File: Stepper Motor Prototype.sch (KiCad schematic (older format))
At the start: 64 parts, among them J1 USB_B_Micro, J2 Screw_Terminal_01x02, J3 Screw_Terminal_01x04, Q1 STD20NF06L, Q2 STD20NF06L, Q3 STD20NF06L, Q4 STD20NF06L, Q5 STD20NF06L, Q6 STD20NF06L, Q7 STD20NF06L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

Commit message: added logic level shifters
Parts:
- removed C16: C, Capacitors_SMD:C_0603_HandSoldering, symbol Device:C
- removed C17, C18, C19, C20, C21, C22, C23, C24: 0.1uF, Capacitors_SMD:C_0603_HandSoldering, symbol Device:C
- removed D1: SP0502BAHT, TO_SOT_Packages_SMD:SOT-23, symbol Power_Protection:SP0502BAHT
- removed D2: TX_LED, LEDs:LED_1206_HandSoldering, symbol Device:LED
- removed D3: RX_LED, LEDs:LED_1206_HandSoldering, symbol Device:LED
- removed D4: D_Schottky, digikey-footprints:DO-214AB, symbol Device:D_Schottky
- removed D5: LED, LEDs:LED_1206_HandSoldering, symbol Device:LED
- removed J1: USB_B_Micro, Connectors:USB_Mini-B, symbol Connector:USB_B_Micro
- removed L1: 100uH, my_inductors:Wurth_SMD_Inductor_7447709101, symbol Device:L
- removed U1: FT232RL, Housings_SSOP:TSSOP-28_4.4x9.7mm_Pitch0.65mm, symbol Interface_USB:FT232RL
- removed U2: ESP8266EX, Housings_DFN_QFN:QFN-32-1EP_5x5mm_Pitch0.5mm, symbol MCU_Espressif:ESP8266EX
- removed U3: LM2595SX-3.3_NOPB, TO_SOT_Packages_SMD:TO-263-5_TabPin3, symbol Voltage~Regulators:LM2595SX-3.3_NOPB
- removed U5: LM2595SX-5.0_NOPB, TO_SOT_Packages_SMD:TO-263-5_TabPin3, symbol Voltage~Regulators:LM2595SX-5.0_NOPB
- removed U6: S25FL512SAGMFIG11, Housings_SOIC:SOIC-16_3.9x9.9mm_Pitch1.27mm, symbol Memory_Flash_3DP:S25FL512SAGMFIG11
- removed U8: STM32F407VGTx, Housings_QFP:LQFP-100_14x14mm_Pitch0.5mm, symbol MCU_ST_STM32F4:STM32F407VGTx
- removed Y1: Crystal_GND24, Crystals:Crystal_SMD_SeikoEpson_TSX3225-4pin_3.2x2.5mm, symbol Device:Crystal_GND24
- added J1: Conn_01x15, Pin_Headers:Pin_Header_Straight_1x15_Pitch1.27mm, symbol Connector_Generic:Conn_01x15
- added R9: 10k, Resistors_SMD:R_0603_HandSoldering, symbol Device:R
- added U1: LM2595SX-5.0_NOPB, TO_SOT_Packages_SMD:TO-263-5_TabPin3, symbol VoltageRegulators:LM2595SX-5.0_NOPB
- added U2, U3: SN74AXC8T245, Housings_SSOP:TSSOP-24_4.4x7.8mm_Pitch0.65mm, symbol logic_level_shifter_mdg:SN74AXC8T245
- C10: value 4.7uF -> 0.1uF
- C11: value 120uF -> 0.1uF; footprint Capacitors_THT:CP_Radial_D8.0mm_P3.50mm -> Capacitors_SMD:C_0603_HandSoldering
- C12: value 150uF -> 100uF
- C15: value C -> 1uF
- C9: value 0.1uF -> 100uF; footprint Capacitors_SMD:C_0603_HandSoldering -> Capacitors_THT:CP_Radial_D8.0mm_P3.50mm
- R1, R5, R6: value 330R -> 10k
- R3: value 4k7 -> 10k
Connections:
- net labels added: +1V8
- net labels removed: FTDI_BYPASS, ST_P100, ST_P11, ST_P19, ST_P22, ST_P28, ST_P50, ST_P6, ST_P75
- wire segments 208 -> 215
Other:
- moved on the sheet: C1, C2, C4, C5, J2

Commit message: removed power supply, basic layout of 1 motor winding complete
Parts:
- removed C13: 120uF, Capacitors_THT:CP_Radial_D8.0mm_P3.50mm, symbol Device:C
- removed C14: 150uF, Capacitors_THT:CP_Radial_D8.0mm_P3.50mm, symbol Device:C
- removed D6: D_Schottky, digikey-footprints:DO-214AB, symbol Device:D_Schottky
- removed D7: LED, LEDs:LED_1206_HandSoldering, symbol Device:LED
- removed J1: Conn_01x15, Pin_Headers:Pin_Header_Straight_1x15_Pitch1.27mm, symbol Connector_Generic:Conn_01x15
- removed L2: L, my_inductors:Wurth_SMD_Inductor_7447709101, symbol Device:L
- removed R2: 330R, Resistors_SMD:R_0603_HandSoldering, symbol Device:R
- removed U1: LM2595SX-5.0_NOPB, TO_SOT_Packages_SMD:TO-263-5_TabPin3, symbol VoltageRegulators:LM2595SX-5.0_NOPB
- added J1: Conn_01x16, symbol Connector_Generic:Conn_01x16
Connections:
- net +1V8: now also J1.2 (Pin_2)
- net +3V3: now also J1.3 (Pin_3)
- net GND: now also J1.1 (Pin_1)
- net AOUT2: now reaches J3.2 (Pin_2), Q3.2 (D), Q4.3 (S), U7.30 (AOUT2)
- net A2HS: now reaches Q4.1 (G), U7.31 (A2HS)
- net A2LS: now reaches Q3.1 (G), U7.32 (A2LS)
- net A1SENP: now reaches Q2.3 (S), Q3.3 (S), R7.1, U7.34 (AISENP)
- net A1LS: now reaches Q2.1 (G), U7.35 (A1LS)
- net A1HS: now reaches Q1.1 (G), U7.36 (A1HS)
- net AOUT1: now reaches J3.1 (Pin_1), Q1.3 (S), Q2.2 (D), U7.37 (AOUT1)
- net at U2.8 (A6): now also J1.11 (Pin_11)
- net at U2.7 (A5): now also J1.12 (Pin_12)
- net at U2.6 (A4): now also J1.13 (Pin_13)
- net at U2.5 (A3): now also J1.14 (Pin_14)
- net at U2.4 (A2): now also J1.15 (Pin_15)
- net at U2.3 (A1): now also J1.16 (Pin_16)
- net at U3.9 (A7): now also J1.4 (Pin_4)
- net at U3.8 (A6): now also J1.5 (Pin_5)
- net at U3.7 (A5): now also J1.6 (Pin_6)
- net at U3.6 (A4): now also J1.7 (Pin_7)
- net at U3.5 (A3): now also J1.8 (Pin_8)
- net at U3.4 (A2): now also J1.9 (Pin_9)
- net at U3.3 (A1): now also J1.10 (Pin_10)
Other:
- moved on the sheet: J2

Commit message: continued working on motor power section.  Still need to layout mirrored side.
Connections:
- net at Q6.3 (S), Q7.3 (S), R8.1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: no longer J3.4 (Pin_4), U7.21 (BOUT2)
- net at Q7.2 (D), Q8.3 (S): now also J3.4 (Pin_4), U7.21 (BOUT2)
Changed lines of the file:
@@
 	24350 8900 24350 8950
 Wire Wire Line
-	25650 9650 25650 7300
-Wire Wire Line
 	25650 7300 25950 7300
 Wire Wire Line
@@
 	21800 7700 22250 7700
 Wire Wire Line
-	22250 7700 22250 9400
-Wire Wire Line
-	22250 9400 24350 9400
-Connection ~ 24350 9400
-Wire Wire Line
-	24350 9400 24350 9350
-Wire Wire Line
-	24350 10200 24350 10350
-Wire Wire Line
-	25650 9650 24350 9650
-Connection ~ 24350 9650
-Wire Wire Line
-	24350 9650 24350 9500
+	24350 10200 24350 10250
 Connection ~ 24350 9750
-Wire Wire Line
-	24350 9750 24350 9650
 $Comp
 L power:GND #PWR0133
@@
 	22800 9500 24350 9500
 Connection ~ 24350 9500
-Wire Wire Line
-	24350 9500 24350 9400
 Wire Wire Line
 	23900 9750 23900 9600
@@
 Text Label 21900 6800 0    50   ~ 0
 AOUT2
+Wire Wire Line
+	24350 9500 24350 9750
+Wire Wire Line
+	25650 10250 24350 10250
+Wire Wire Line
+	25650 7300 25650 10250
+Connection ~ 24350 10250
+Wire Wire Line
+	24350 10250 24350 10350
+Wire Wire Line
+	24350 9350 24350 9500
+Wire Wire Line
+	22250 10250 24350 10250
+Wire Wire Line
+	22250 7700 22250 10250
 $EndSCHEMATC

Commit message: traces are all connected, still need to refine routing of logic side
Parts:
- removed J1: Conn_01x16, symbol Connector_Generic:Conn_01x16
- added J1: Conn_01x19, Pin_Headers:Pin_Header_Straight_1x19_Pitch2.54mm, symbol Connector_Generic:Conn_01x19
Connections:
- net +1V8: now also J1.17 (Pin_17), J1.3 (Pin_3)
- net +3V3: now also J1.18 (Pin_18), J1.2 (Pin_2)
- net GND: now also J1.1 (Pin_1), J1.19 (Pin_19)
- net at U2.3 (A1): now also J1.16 (Pin_16)
- net at U2.4 (A2): now also J1.15 (Pin_15)
- net at U2.5 (A3): now also J1.14 (Pin_14)
- net at U2.6 (A4): now also J1.13 (Pin_13)
- net at U2.7 (A5): now also J1.12 (Pin_12)
- net at U2.8 (A6): now also J1.11 (Pin_11)
- net at U3.3 (A1): now also J1.10 (Pin_10)
- net at U3.4 (A2): now also J1.9 (Pin_9)
- net at U3.5 (A3): now also J1.8 (Pin_8)
- net at U3.6 (A4): now also J1.7 (Pin_7)
- net at U3.7 (A5): now also J1.6 (Pin_6)
- net at U3.8 (A6): now also J1.5 (Pin_5)
- net at U3.9 (A7): now also J1.4 (Pin_4)
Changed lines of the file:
@@
 	15900 10550 14300 10550
-Wire Wire Line
-	14300 10550 14300 9250
-Wire Wire Line
-	14300 9250 13250 9250
 Wire Wire Line
 	15900 10650 14250 10650
 Wire Wire Line
-	14250 10650 14250 9350
-Wire Wire Line
-	14250 9350 13250 9350
-Wire Wire Line
 	15900 10750 14200 10750
-Wire Wire Line
-	14200 10750 14200 9450
-Wire Wire Line
-	14200 9450 13250 9450
 Wire Wire Line
 	15900 10850 14150 10850
 Wire Wire Line
-	14150 10850 14150 9550
-Wire Wire Line
-	14150 9550 13250 9550
-Wire Wire Line
 	15900 10950 14100 10950
-Wire Wire Line
-	14100 10950 14100 9650
-Wire Wire Line
-	14100 9650 13250 9650
 Wire Wire Line
 	15900 11050 14050 11050
 Wire Wire Line
-	14050 11050 14050 9750
-Wire Wire Line
-	14050 9750 13250 9750
-Wire Wire Line
 	15900 11150 14000 11150
-Wire Wire Line
-	14000 11150 14000 9850
-Wire Wire Line
-	14000 9850 13250 9850
 Connection ~ 24350 3000
 Wire Wire Line
 	24350 3000 24350 2800
 $Comp
-L Connector_Generic:Conn_01x16 J1
-U 1 1 5C986280
-P 13050 9450
-F 0 "J1" H 12970 8425 50  0000 C CNN
-F 1 "Conn_01x16" H 12970 8516 50  0000 C CNN
-F 2 "" H 13050 9450 50  0001 C CNN
-F 3 "~" H 13050 9450 50  0001 C CNN
-	1    13050 9450
-	-1   0    0    1
-$EndComp
-$Comp
 L power:+3.3V #PWR0109
 U 1 1 5C986679
-P 13250 9950
-F 0 "#PWR0109" H 13250 9800 50  0001 C CNN
-F 1 "+3.3V" V 13265 10078 50  0000 L CNN
-F 2 "" H 13250 9950 50  0001 C CNN
-F 3 "" H 13250 9950 50  0001 C CNN
-	1    13250 9950
+P 13250 10050
+F 0 "#PWR0109" H 13250 9900 50  0001 C CNN
+F 1 "+3.3V" V 13265 10178 50  0000 L CNN
+F 2 "" H 13250 10050 50  0001 C CNN
+F 3 "" H 13250 10050 50  0001 C CNN
+	1    13250 10050
 	0    1    1    0
 $EndComp
@@
 L power:+1V8 #PWR0111
 U 1 1 5C986A2C
-P 13250 10050
-F 0 "#PWR0111" H 13250 9900 50  0001 C CNN
-F 1 "+1V8" V 13265 10178 50  0000 L CNN
-F 2 "" H 13250 10050 50  0001 C CNN
-F 3 "" H 13250 10050 50  0001 C CNN
-	1    13250 10050
+P 13250 9950
+F 0 "#PWR0111" H 13250 9800 50  0001 C CNN
+F 1 "+1V8" V 13265 10078 50  0000 L CNN
+F 2 "" H 13250 9950 50  0001 C CNN
+F 3 "" H 13250 9950 50  0001 C CNN
+	1    13250 9950
 	0    1    1    0
 $EndComp
@@
 Wire Wire Line
 	22250 7700 22250 10250
+$Comp
+L Connector_Generic:Conn_01x19 J1
+U 1 1 5C7B8F84
+P 13050 9250
+F 0 "J1" H 12970 8125 50  0000 C CNN
+F 1 "Conn_01x19" H 12970 8216 50  0000 C CNN
+F 2 "Pin_Headers:Pin_Header_Straight_1x19_Pitch2.54mm" H 13050 9250 50  0001 C CNN
+F 3 "~" H 13050 9250 50  0001 C CNN
+	1    13050 9250
+	-1   0    0    1
+$EndComp
+$Comp
+L power:GND #PWR0113
+U 1 1 5C7B92E9
+P 13250 8350
+F 0 "#PWR0113" H 13250 8100 50  0001 C CNN
+F 1 "GND" V 13255 8177 50  0000 C CNN
+F 2 "" H 13250 8350 50  0001 C CNN
+F 3 "" H 13250 8350 50  0001 C CNN
+	1    13250 8350
+	0    -1   1    0
+$EndComp
+$Comp
+L power:+3.3V #PWR0114
+U 1 1 5C7B92EF
+P 13250 8450
+F 0 "#PWR0114" H 13250 8300 50  0001 C CNN
+F 1 "+3.3V" V 13265 8578 50  0000 L CNN
+F 2 "" H 13250 8450 50  0001 C CNN
+F 3 "" H 13250 8450 50  0001 C CNN
+	1    13250 8450
+	0    1    -1   0
+$EndComp
+$Comp
+L power:+1V8 #PWR0123
+U 1 1 5C7B92F5
+P 13250 8550
+F 0 "#PWR0123" H 13250 8400 50  0001 C CNN
+F 1 "+1V8" V 13265 8678 50  0000 L CNN
+F 2 "" H 13250 8550 50  0001 C CNN
+F 3 "" H 13250 8550 50  0001 C CNN
+	1    13250 8550
+	0    1    -1   0
+$EndComp
+Wire Wire Line
+	14300 10550 14300 9250
+Wire Wire Line
+	14300 9250 13250 9250
+Wire Wire Line
+	13250 9350 14250 9350
+Wire Wire Line
+	14250 9350 14250 10650
+Wire Wire Line
+	14200 10750 14200 9450
+Wire Wire Line
+	14200 9450 13250 9450
+Wire Wire Line
+	13250 9550 14150 9550
+Wire Wire Line
+	14150 9550 14150 10850
+Wire Wire Line
+	14100 10950 14100 9650
+Wire Wire Line
+	14100 9650 13250 9650
+Wire Wire Line
+	13250 9750 14050 9750
+Wire Wire Line
+	14050 9750 14050 11050
+Wire Wire Line
+	14000 9850 13250 9850
+Wire Wire Line
+	14000 9850 14000 11150
 $EndSCHEMATC

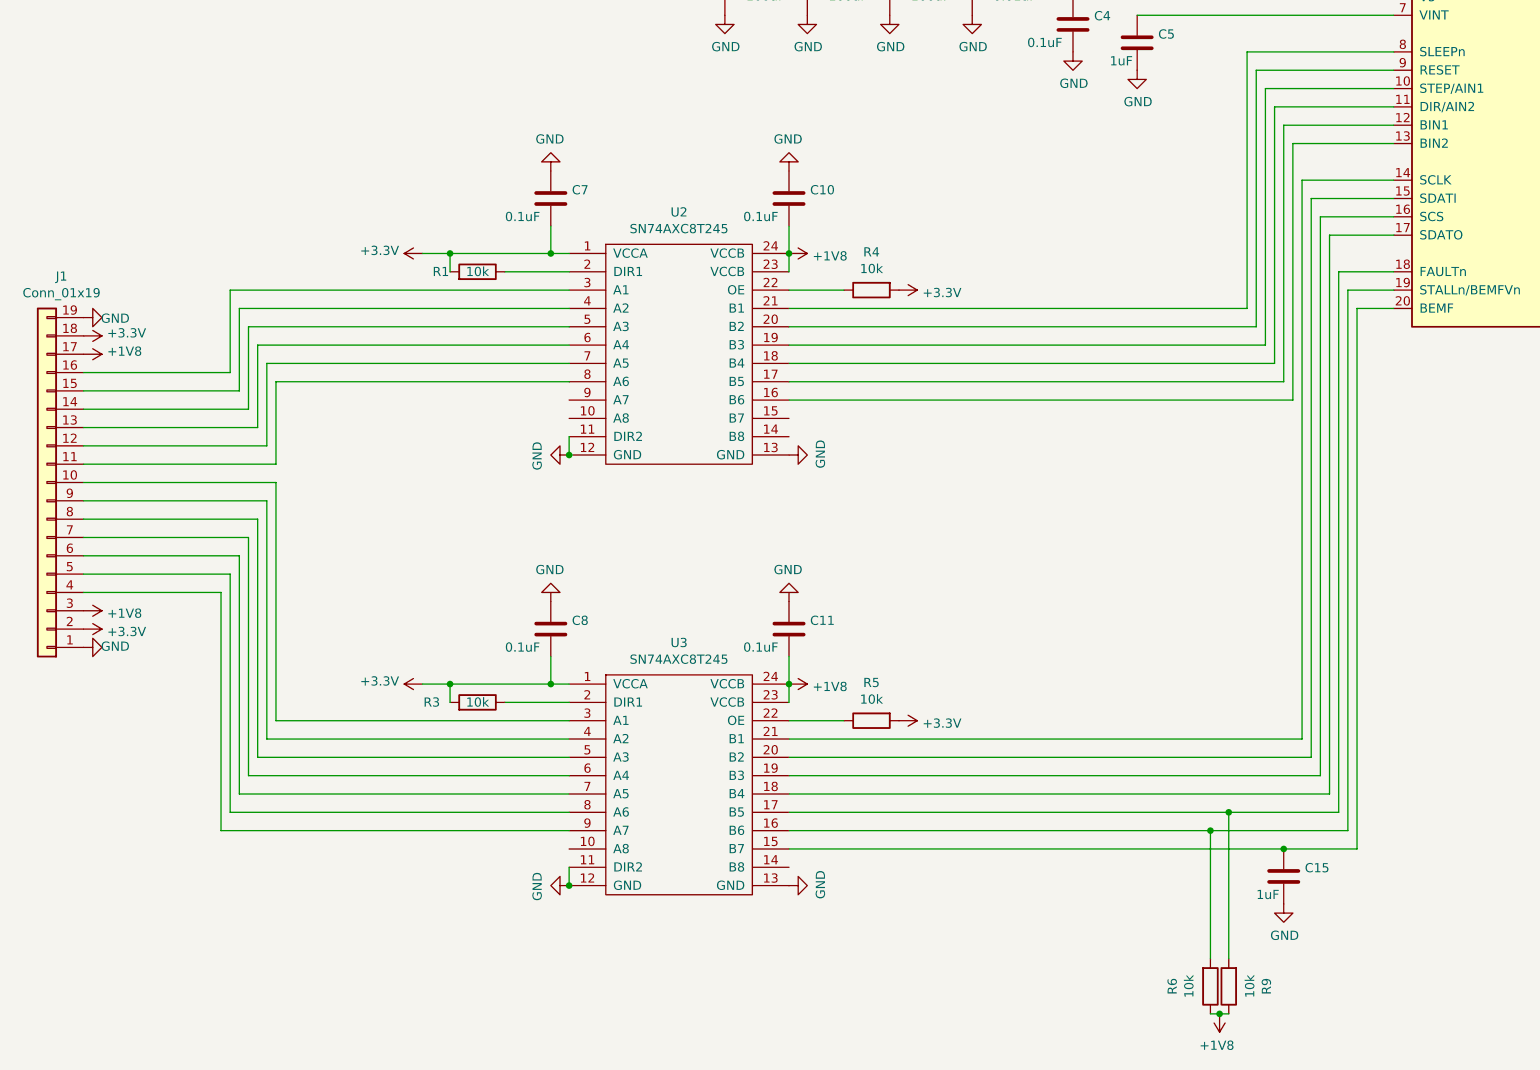
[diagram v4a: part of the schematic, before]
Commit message: removed voltage level translator, all nets are connected
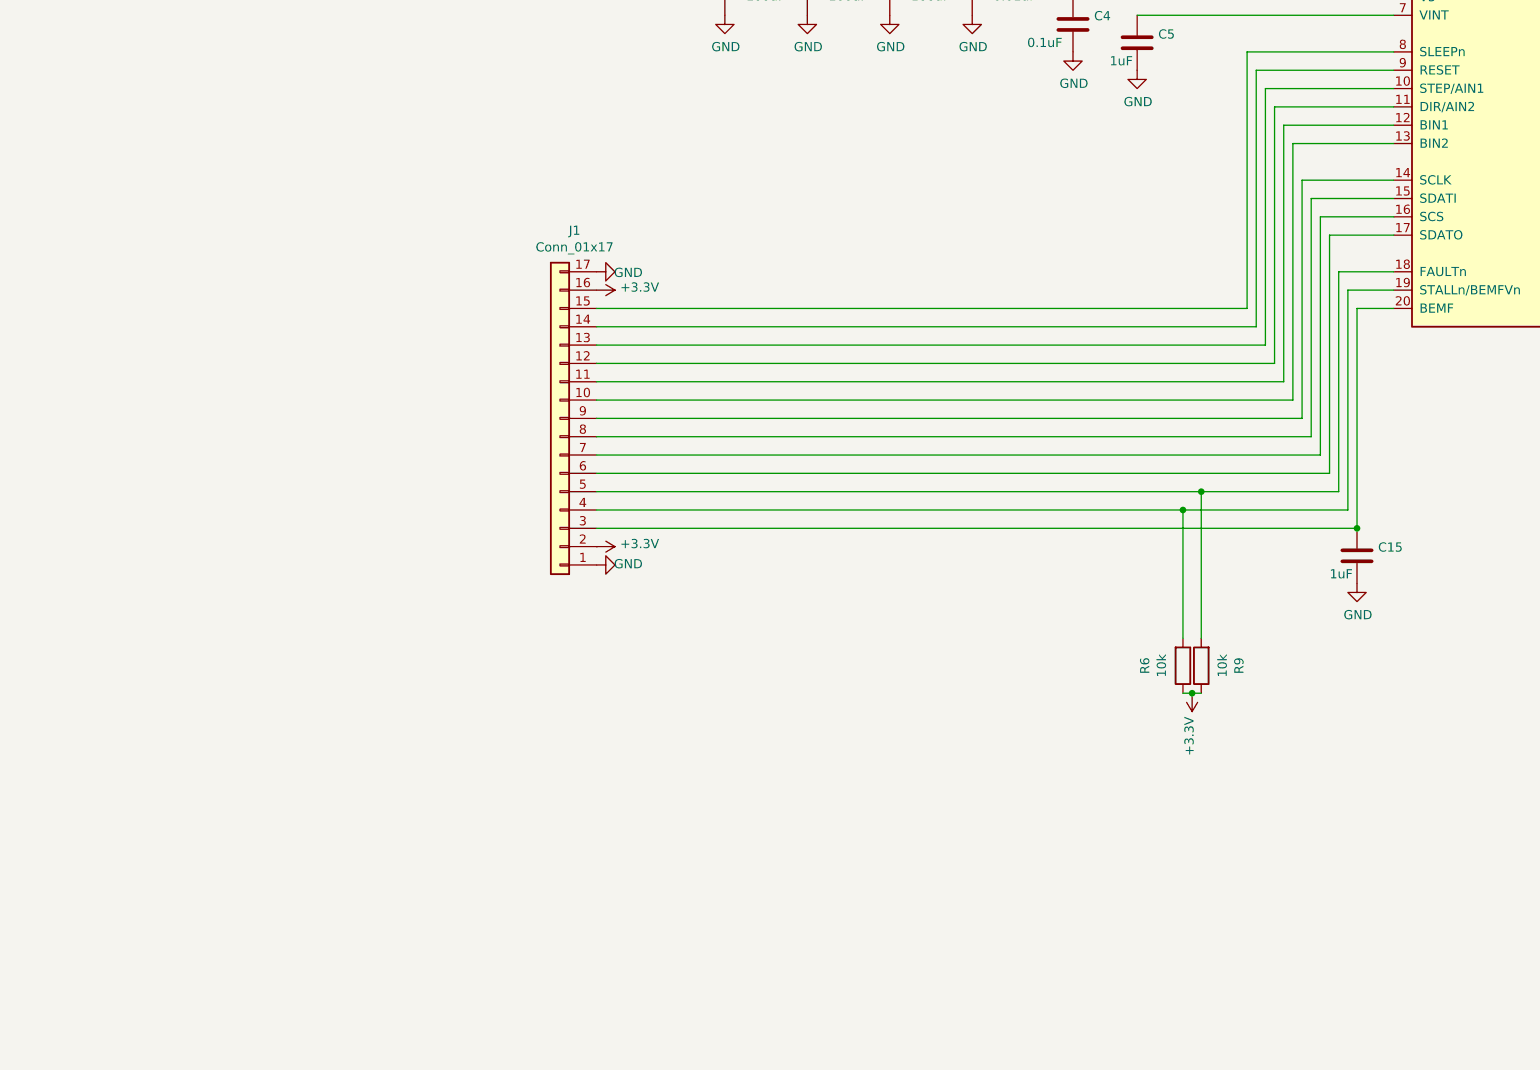
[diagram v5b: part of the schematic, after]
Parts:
- removed C10, C11, C7, C8: 0.1uF, Capacitors_SMD:C_0603_HandSoldering, symbol Device:C
- removed J1: Conn_01x19, Pin_Headers:Pin_Header_Straight_1x19_Pitch2.54mm, symbol Connector_Generic:Conn_01x19
- removed R1, R3, R4, R5: 10k, Resistors_SMD:R_0603_HandSoldering, symbol Device:R
- removed U2, U3: SN74AXC8T245, Housings_SSOP:TSSOP-24_4.4x7.8mm_Pitch0.65mm, symbol logic_level_shifter_mdg:SN74AXC8T245
- added J1: Conn_01x17, Pin_Headers:Pin_Header_Straight_1x17_Pitch2.54mm, symbol Connector_Generic:Conn_01x17
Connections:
- net +1V8 is gone; now on net +3V3: R6.1, R9.1
- net +3V3: now also J1.16 (Pin_16), J1.2 (Pin_2)
- net GND: now also J1.1 (Pin_1), J1.17 (Pin_17)
- net at U7.10 (STEP/AIN1): now also J1.13 (Pin_13)
- net at U7.11 (DIR/AIN2): now also J1.12 (Pin_12)
- net at U7.12 (BIN1): now also J1.11 (Pin_11)
- net at U7.13 (BIN2): now also J1.10 (Pin_10)
- net at U7.14 (SCLK): now also J1.9 (Pin_9)
- net at U7.15 (SDATI): now also J1.8 (Pin_8)
- net at U7.16 (SCS): now also J1.7 (Pin_7)
- net at U7.17 (SDATO): now also J1.6 (Pin_6)
- net at R9.2, U7.18 (FAULTn): now also J1.5 (Pin_5)
- net at R6.2, U7.19 (STALLn/BEMFVn): now also J1.4 (Pin_4)
- net at C15.1, U7.20 (BEMF): now also J1.3 (Pin_3)
- net at U7.8 (SLEEPn): now also J1.15 (Pin_15)
- net at U7.9 (RESET): now also J1.14 (Pin_14)
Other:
- moved on the sheet: C15, R6, R9
